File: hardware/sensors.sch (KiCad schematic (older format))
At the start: 0 parts

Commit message: the inputs and power are don for shematic.
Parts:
- added U?: AM2302, symbol AM2302
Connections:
- new net +5V: U?.1 (VDD)
- new net AM2302Out: U?.2 (SDA)
- new net GND: U?.4 (GND)
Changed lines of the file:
@@
 LIBS:contrib
 LIBS:valves
-LIBS:arduino
-LIBS:ESP8266
 LIBS:LDD1500H
-LIBS:jardinio-cache
 EELAYER 25 0
 EELAYER END
 $Descr A4 11693 8268
 encoding utf-8
-Sheet 1 5
+Sheet 1 1
 Title ""
 Date ""
@@
 Comment4 ""
 $EndDescr
+$Comp
+L AM2302 U?
+U 1 1 5AC2DA54
+P 1400 1750
+F 0 "U?" H 1150 2650 60  0000 C CNN
+F 1 "AM2302" H 1150 2650 60  0000 C CNN
+F 2 "" H 1150 2650 60  0000 C CNN
+F 3 "" H 1150 2650 60  0000 C CNN
+	1    1400 1750
+	1    0    0    -1
+$EndComp
+$Comp
+L +5V #PWR?
+U 1 1 5AC2DBA5
+P 1400 800
+F 0 "#PWR?" H 1400 650 50  0001 C CNN
+F 1 "+5V" H 1400 940 50  0000 C CNN
+F 2 "" H 1400 800 50  0000 C CNN
+F 3 "" H 1400 800 50  0000 C CNN
+	1    1400 800
+	1    0    0    -1
+$EndComp
+$Comp
+L GND #PWR?
+U 1 1 5AC2DBBB
+P 1400 1700
+F 0 "#PWR?" H 1400 1450 50  0001 C CNN
+F 1 "GND" H 1400 1550 50  0000 C CNN
+F 2 "" H 1400 1700 50  0000 C CNN
+F 3 "" H 1400 1700 50  0000 C CNN
+	1    1400 1700
+	1    0    0    -1
+$EndComp
+Text HLabel 2450 1250 2    60   Output ~ 0
+AM2302Out
+Text Label 1900 1250 0    60   ~ 0
+AM2302Out
+Wire Wire Line
+	1850 1250 2450 1250
+Wire Wire Line
+	1400 1650 1400 1700
+Wire Wire Line
+	1400 850  1400 800
 $EndSCHEMATC

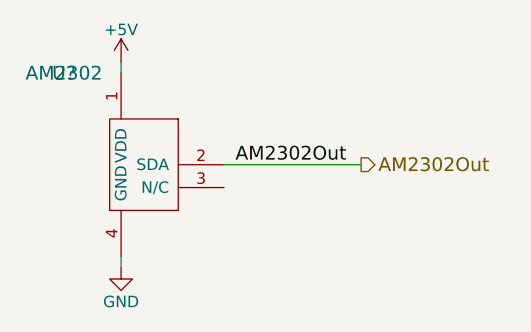
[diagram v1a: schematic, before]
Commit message: sheets are named, global circuit is done.
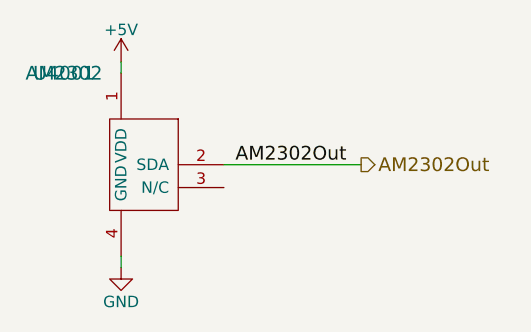
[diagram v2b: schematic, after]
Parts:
- gave numbers to parts that had none: 1
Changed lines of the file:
@@
 LIBS:contrib
 LIBS:valves
+LIBS:arduino
+LIBS:ESP8266
 LIBS:LDD1500H
+LIBS:jardinio-cache
 EELAYER 25 0
 EELAYER END
 $Descr A4 11693 8268
 encoding utf-8
-Sheet 1 1
-Title ""
-Date ""
-Rev ""
-Comp ""
+Sheet 1 5
+Title "jardinIO circuit"
+Date "2018-04-18"
+Rev "0"
+Comp "Cedille"
 Comment1 ""
 Comment2 ""
@@
 $EndDescr
 $Comp
-L AM2302 U?
+L AM2302 U4001
 U 1 1 5AC2DA54
 P 1400 1750
-F 0 "U?" H 1150 2650 60  0000 C CNN
+F 0 "U4001" H 1150 2650 60  0000 C CNN
 F 1 "AM2302" H 1150 2650 60  0000 C CNN
 F 2 "" H 1150 2650 60  0000 C CNN
@@
 $EndComp
 $Comp
-L +5V #PWR?
+L +5V #PWR012
 U 1 1 5AC2DBA5
 P 1400 800
-F 0 "#PWR?" H 1400 650 50  0001 C CNN
+F 0 "#PWR012" H 1400 650 50  0001 C CNN
 F 1 "+5V" H 1400 940 50  0000 C CNN
 F 2 "" H 1400 800 50  0000 C CNN
@@
 $EndComp
 $Comp
-L GND #PWR?
+L GND #PWR013
 U 1 1 5AC2DBBB
 P 1400 1700
-F 0 "#PWR?" H 1400 1450 50  0001 C CNN
+F 0 "#PWR013" H 1400 1450 50  0001 C CNN
 F 1 "GND" H 1400 1550 50  0000 C CNN
 F 2 "" H 1400 1700 50  0000 C CNN
